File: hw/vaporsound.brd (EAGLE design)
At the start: 100 x 80 mm, 76 parts, among them Q1 BSS138, Q2 BSS138

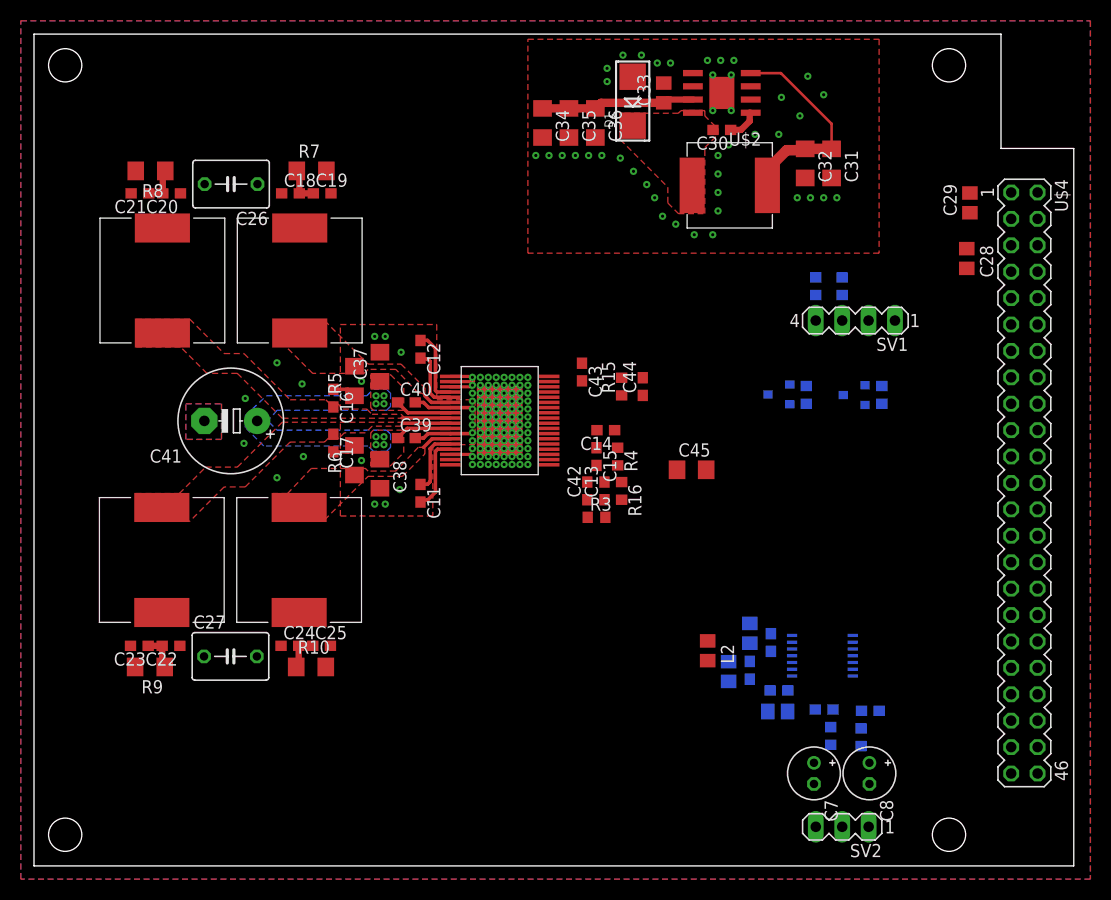
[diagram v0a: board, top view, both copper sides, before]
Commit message: output stage fully routed, adc routed
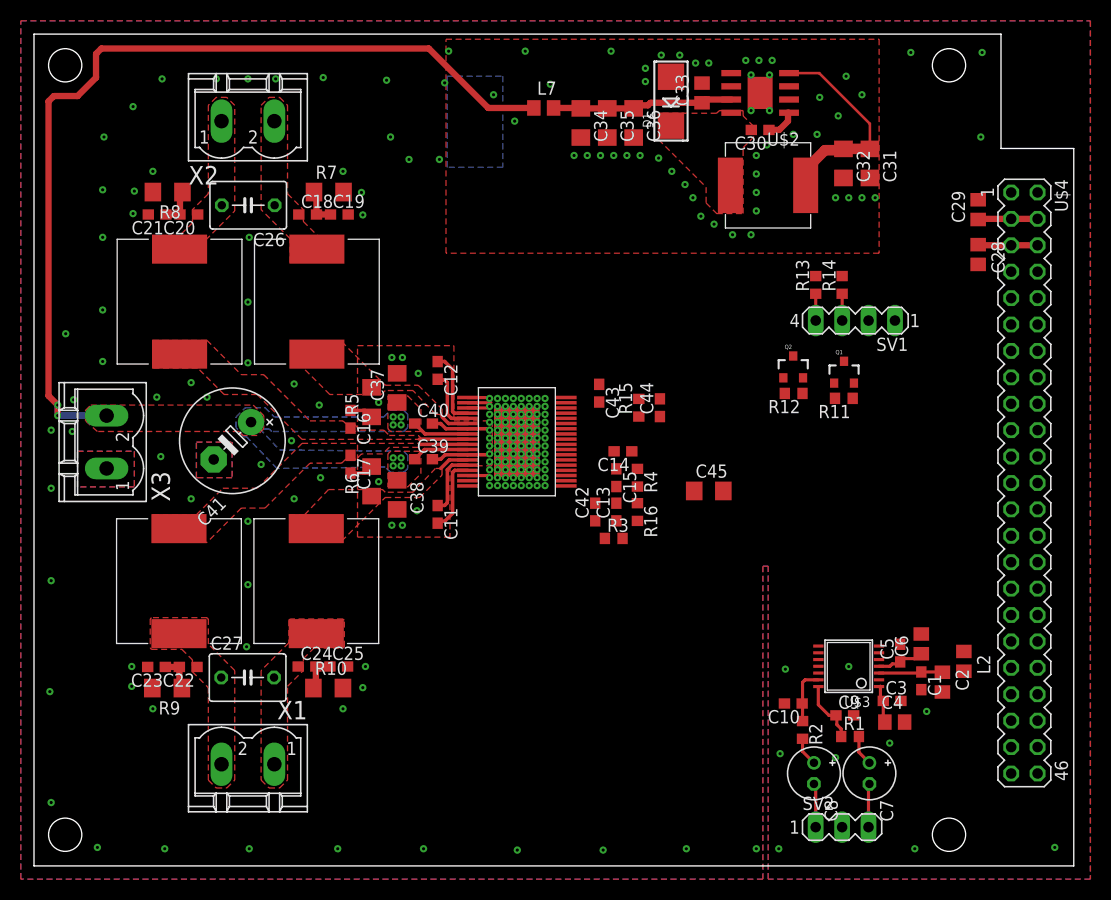
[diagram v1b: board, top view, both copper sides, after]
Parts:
- added L7: (no value), rcl:R0805
- added X1, X2, X3: MSTBV2, con-phoenix-508:MSTBV2
- moved L2 24.7 mm to (89.4, 19.7)
- moved C2 20.6 mm to (87.4, 17.7), flipped to the top
- moved C1 16.5 mm to (85.3, 17.8), flipped to the top
- moved C6 16.5 mm to (85.3, 21.4), flipped to the top
- moved C5 12.5 mm to (83.3, 20.5), flipped to the top
- moved C4 11.3 mm to (82.8, 13.8), flipped to the top
- moved C3 10.9 mm to (82.5, 15.9), flipped to the top
- moved C10 7.44 mm to (73.0, 15.6), flipped to the top
- moved R2 5.68 mm to (73.9, 13.1), flipped to the top
- moved C7 5.33 mm to (80.3, 8.90)
- moved C8 5.33 mm to (75.0, 8.90)
- moved C31 3.68 mm to (80.4, 67.6)
- moved C34 3.68 mm to (52.6, 71.5)
- moved C33 3.68 mm to (64.2, 74.3)
- moved C35 3.68 mm to (55.1, 71.5)
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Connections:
- new net 24V_DIGITAL: C33.1, C34.1, C35.1, C36.1, L7.2, U$2.7
- net +24V: now also L7.1, X3.2; no longer C33.1, C34.1, C35.1, C36.1, U$2.7
- net GND: now also X3.1
- net SPKR1A: now also X1.1
- net SPKR1B: now also X1.2
- net SPKR2A: now also X2.1
- net SPKR2B: now also X2.2
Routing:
- net +24V: track 25.8 -> 99.7 mm, vias 8 -> 10
- net 24V_DIGITAL: track 0.00 -> 17.5 mm
- net +3V3: track 0.00 -> 10.3 mm
- net V+: track 0.00 -> 6.15 mm
- net VIN_R: track 0.00 -> 6.11 mm
- net +5V: track 20.7 -> 26.5 mm
- net VIN_L: track 0.00 -> 5.38 mm
- net LEFT_INPUT: track 0.00 -> 4.22 mm
- net RIGHT_INPUT: track 0.00 -> 4.19 mm
- net ADC_VREF: track 0.00 -> 3.76 mm
- net C_RIGHT: track 0.00 -> 2.95 mm
- net C_LEFT: track 0.00 -> 2.77 mm
- net SDA5V: track 0.00 -> 2.58 mm
- net SCL5V: track 0.00 -> 2.58 mm
- net GND: vias 152 -> 226
- added copper zone on layer 1, net SPKR1A
- added copper zone on layer 1, net SPKR1B
- added copper zone on layer 1, net SPKR2A
- added copper zone on layer 1, net SPKR2B

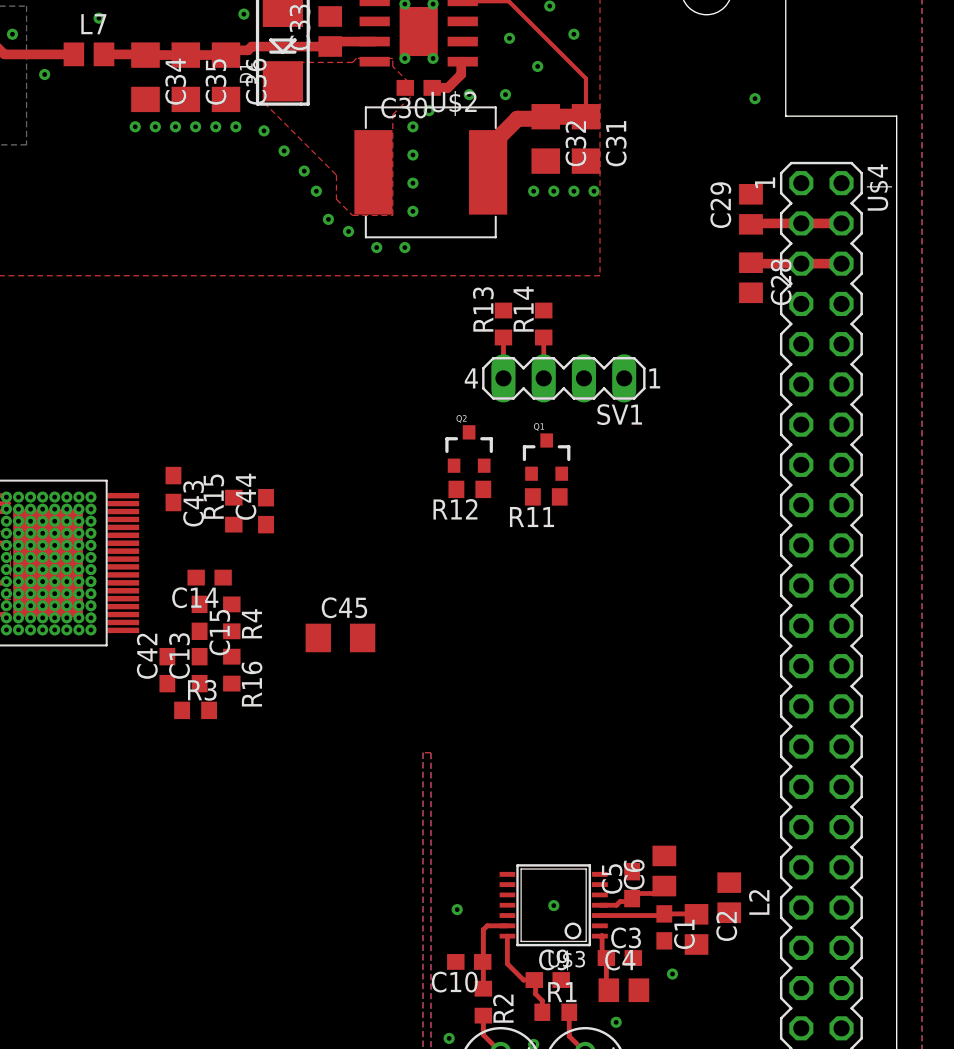
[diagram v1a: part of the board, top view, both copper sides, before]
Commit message: board fully routed
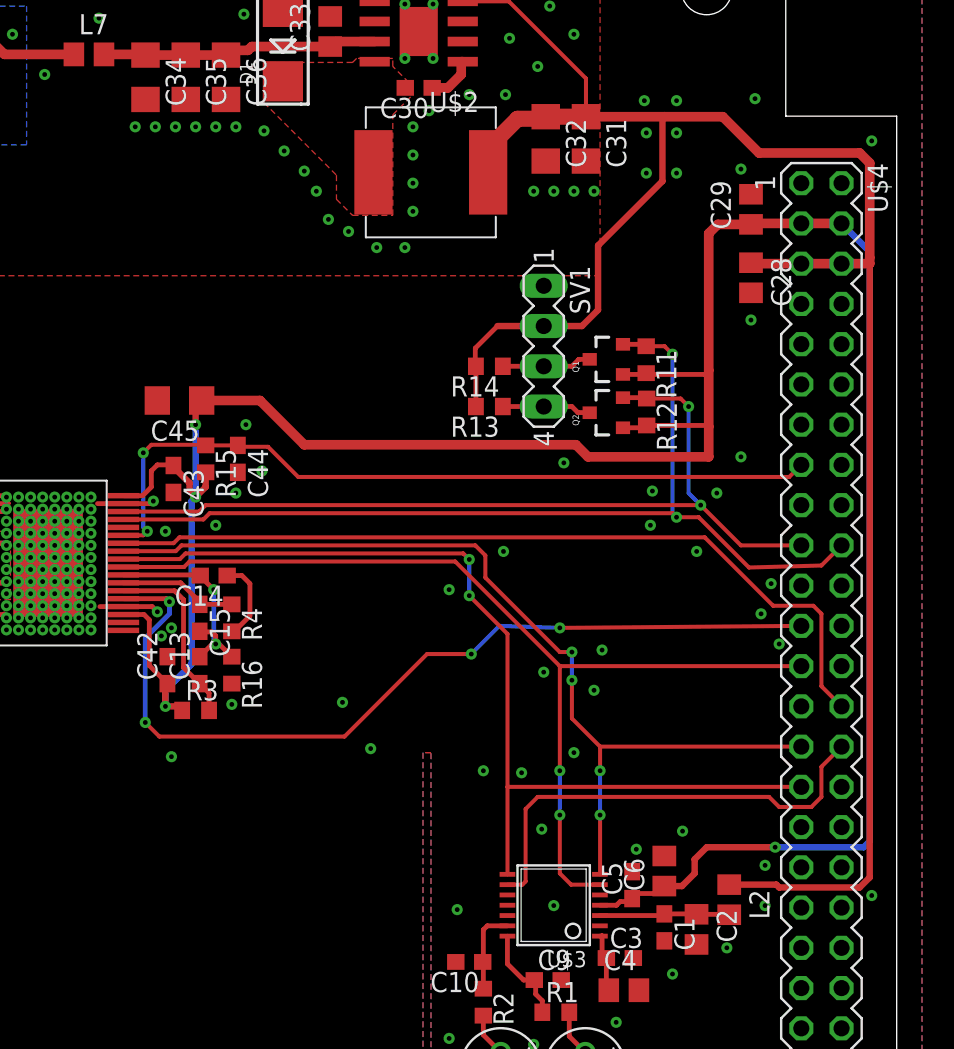
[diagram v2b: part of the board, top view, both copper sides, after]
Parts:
- moved C45 18.1 mm to (54.7, 51.1), turned to 180 degrees
- moved R12 12.2 mm to (84.2, 50.3), turned to 270 degrees
- moved R11 10.7 mm to (84.2, 53.6), turned to 270 degrees
- moved Q2 9.02 mm to (81.7, 50.3), turned to 90 degrees
- moved Q1 7.30 mm to (81.7, 53.6), turned to 90 degrees
- moved R13 5.28 mm to (74.3, 50.7), turned to 180 degrees
- moved R14 4.34 mm to (74.3, 53.2), turned to 180 degrees
- moved C44 3.75 mm to (58.4, 47.4), turned to 270 degrees
- moved R15 3.75 mm to (56.4, 47.4), turned to 270 degrees
- moved SV1 2.40 mm to (77.7, 54.5), turned to 270 degrees
- moved C43 0.63 mm to (54.4, 46.1)
- moved C14 0.28 mm to (56.9, 40.0)
- moved L2 0.13 mm to (89.4, 19.6)
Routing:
- net +3V3: track 10.3 -> 164.7 mm, vias 0 -> 4
- net +5V: track 26.5 -> 128.4 mm
- net MCK: track 0.00 -> 61.6 mm, vias 0 -> 2
- net BCK: track 0.00 -> 61.6 mm, vias 0 -> 2
- net SDA: track 0.00 -> 61.2 mm, vias 0 -> 2
- net LRCK: track 0.00 -> 59.5 mm, vias 0 -> 4
- net POWERDOWN: track 0.00 -> 55.9 mm, vias 0 -> 4
- net SCL: track 0.00 -> 54.9 mm, vias 0 -> 2
- net D_AMP: track 0.00 -> 52.6 mm
- net RESET: track 0.00 -> 49.6 mm, vias 0 -> 2
- net D_ADC: track 0.00 -> 29.0 mm
- net AGND: track 0.00 -> 13.9 mm, vias 0 -> 2
- net VDD_PLL: track 0.00 -> 11.7 mm
- net FILTER_PLL: track 0.00 -> 7.51 mm
- net GND: track 19.8 -> 27.2 mm, vias 226 -> 272
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
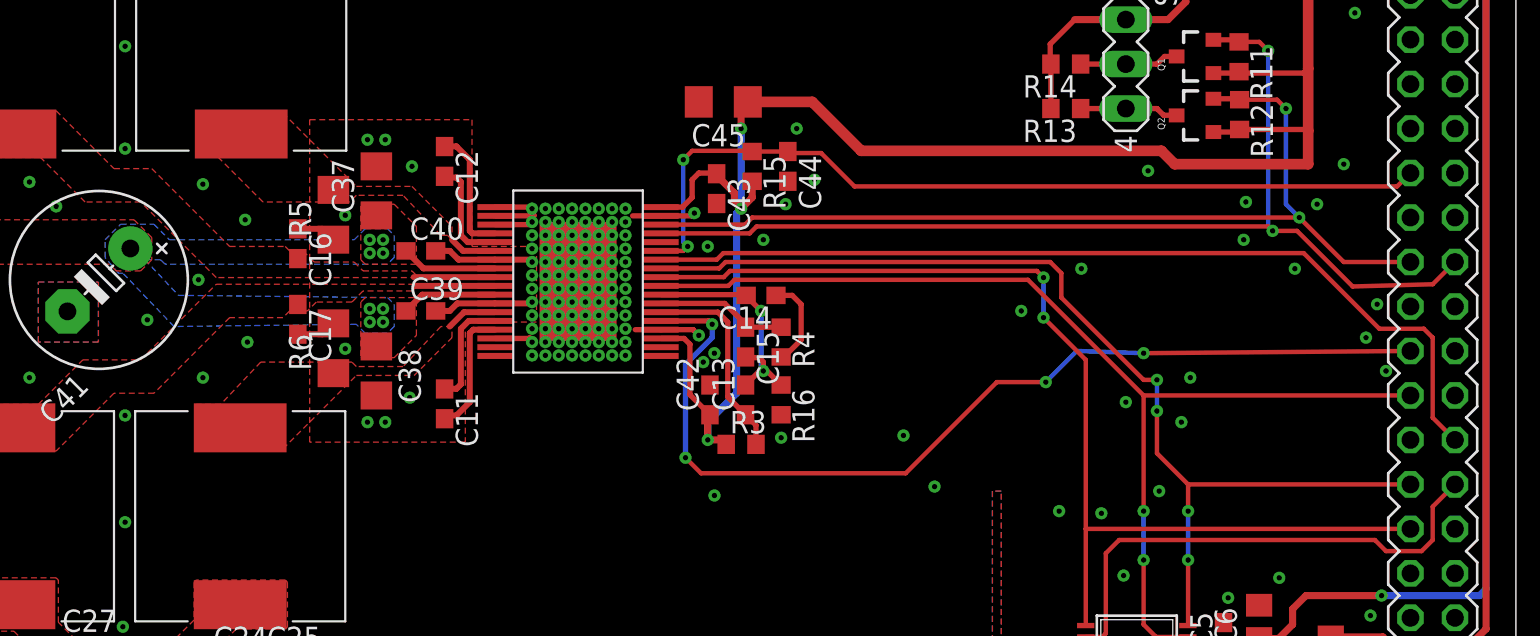
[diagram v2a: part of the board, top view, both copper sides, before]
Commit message: fix wrong angles
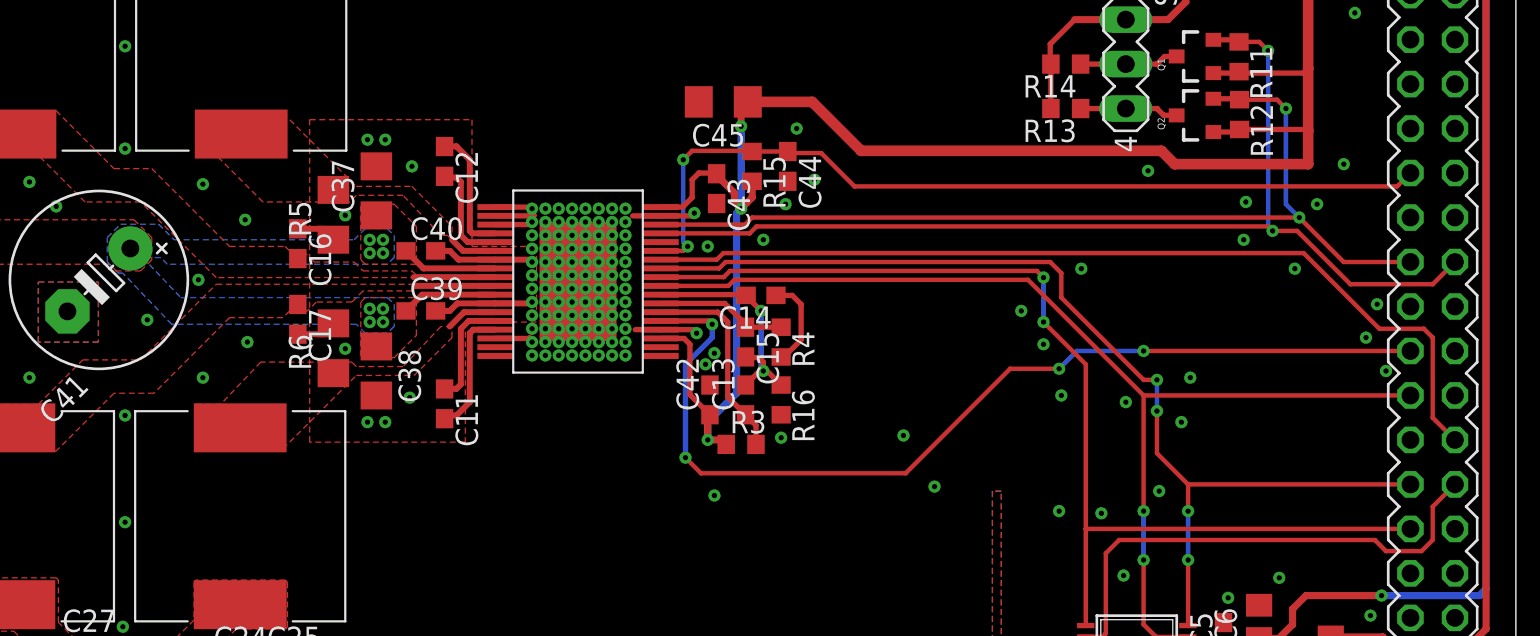
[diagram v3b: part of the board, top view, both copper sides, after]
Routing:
- net GND: track 27.2 -> 27.0 mm, vias 272 -> 274
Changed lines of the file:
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@@
 <via x="78.359" y="19.177" extent="1-16" drill="0.3"/>
 <via x="85.852" y="14.859" extent="1-16" drill="0.3"/>
-<via x="53.594" y="36.195" extent="1-16" drill="0.3"/>
-<via x="53.34" y="37.719" extent="1-16" drill="0.3"/>
+<via x="53.721" y="36.068" extent="1-16" drill="0.3"/>
+<via x="53.213" y="37.846" extent="1-16" drill="0.3"/>
 <via x="54.229" y="36.703" extent="1-16" drill="0.3"/>
 <wire x1="51.191" y1="38.046" x2="53.013" y2="38.046" width="0.3048" layer="1"/>
-<wire x1="53.013" y1="38.046" x2="53.34" y2="37.719" width="0.3048" layer="1"/>
+<wire x1="53.013" y1="38.046" x2="53.213" y2="37.846" width="0.3048" layer="1"/>
 <wire x1="49.711" y1="38.046" x2="51.191" y2="38.046" width="0.3048" layer="1"/>
 <via x="53.086" y="44.704" extent="1-16" drill="0.3"/>
@@
 <via x="66.802" y="29.083" extent="1-16" drill="0.3"/>
 <via x="65.024" y="32.004" extent="1-16" drill="0.3"/>
+<via x="74.041" y="34.29" extent="1-16" drill="0.3"/>
+<via x="73.025" y="37.211" extent="1-16" drill="0.3"/>
 </signal>
 <signal name="EPAD">
@@
 <wire x1="55.499" y1="34.417" x2="55.499" y2="44.704" width="0.4064" layer="16"/>
 <wire x1="55.499" y1="44.704" x2="55.753" y2="44.958" width="0.4064" layer="16"/>
-<wire x1="55.753" y1="44.958" x2="55.753" y2="49.53" width="0.4064" layer="16"/>
+<wire x1="55.753" y1="44.958" x2="55.753" y2="49.657" width="0.4064" layer="16"/>
 <via x="55.753" y="44.958" extent="1-16" drill="0.3"/>
 <wire x1="56.388" y1="46.521" x2="56.388" y2="45.593" width="0.4064" layer="1"/>
@@
 <wire x1="82.726" y1="52.699" x2="84.108" y2="52.699" width="0.3048" layer="1"/>
 <wire x1="84.108" y1="52.699" x2="84.19" y2="52.781" width="0.3048" layer="1"/>
-<via x="55.753" y="49.53" extent="1-16" drill="0.3"/>
+<via x="55.753" y="49.657" extent="1-16" drill="0.3"/>
 <wire x1="55.753" y1="44.958" x2="55.753" y2="45.173" width="0.4064" layer="1"/>
-<wire x1="55.753" y1="49.53" x2="55.753" y2="50.67" width="0.4064" layer="1"/>
+<wire x1="55.753" y1="49.657" x2="55.753" y2="50.67" width="0.4064" layer="1"/>
 <wire x1="55.753" y1="50.67" x2="56.137" y2="51.054" width="0.4064" layer="1"/>
 <wire x1="56.137" y1="51.054" x2="59.817" y2="51.054" width="0.6096" layer="1"/>
@@
 <wire x1="85.852" y1="43.942" x2="86.106" y2="43.688" width="0.254" layer="1"/>
 <wire x1="86.106" y1="43.688" x2="87.503" y2="43.688" width="0.254" layer="1"/>
-<wire x1="87.503" y1="43.688" x2="90.678" y2="40.513" width="0.254" layer="1"/>
-<wire x1="90.678" y1="40.513" x2="95.25" y2="40.64" width="0.254" layer="1"/>
 <wire x1="95.25" y1="40.64" x2="96.52" y2="41.91" width="0.254" layer="1"/>
 <wire x1="84.19" y1="54.481" x2="85.346" y2="54.481" width="0.254" layer="1"/>
@@
 <wire x1="85.852" y1="43.942" x2="86.106" y2="43.688" width="0.254" layer="16"/>
 <via x="86.106" y="43.688" extent="1-16" drill="0.3"/>
+<wire x1="87.503" y1="43.688" x2="90.551" y2="40.64" width="0.254" layer="1"/>
+<wire x1="90.551" y1="40.64" x2="95.25" y2="40.64" width="0.254" layer="1"/>
 </signal>
 <signal name="RESET">
@@
 <wire x1="54.102" y1="37.592" x2="52.578" y2="36.068" width="0.3048" layer="16"/>
 <wire x1="52.578" y1="36.068" x2="52.578" y2="30.734" width="0.3048" layer="16"/>
-<wire x1="93.98" y1="36.83" x2="78.74" y2="36.703" width="0.254" layer="1"/>
+<wire x1="93.98" y1="36.83" x2="78.74" y2="36.83" width="0.254" layer="1"/>
 <via x="52.578" y="30.734" extent="1-16" drill="0.3"/>
 <wire x1="52.578" y1="30.734" x2="53.467" y2="29.845" width="0.254" layer="1"/>
 <wire x1="53.467" y1="29.845" x2="65.151" y2="29.845" width="0.254" layer="1"/>
-<via x="78.74" y="36.703" extent="1-16" drill="0.3"/>
-<wire x1="78.74" y1="36.703" x2="74.93" y2="36.83" width="0.254" layer="16"/>
-<wire x1="74.93" y1="36.83" x2="73.152" y2="35.052" width="0.254" layer="16"/>
-<via x="73.152" y="35.052" extent="1-16" drill="0.3"/>
-<wire x1="73.152" y1="35.052" x2="70.358" y2="35.052" width="0.254" layer="1"/>
-<wire x1="70.358" y1="35.052" x2="65.151" y2="29.845" width="0.254" layer="1"/>
+<via x="78.74" y="36.83" extent="1-16" drill="0.3"/>
+<wire x1="78.74" y1="36.83" x2="74.93" y2="36.83" width="0.254" layer="16"/>
+<wire x1="74.93" y1="36.83" x2="73.914" y2="35.814" width="0.254" layer="16"/>
+<via x="73.914" y="35.814" extent="1-16" drill="0.3"/>
+<wire x1="73.914" y1="35.814" x2="71.12" y2="35.814" width="0.254" layer="1"/>
+<wire x1="71.12" y1="35.814" x2="65.151" y2="29.845" width="0.254" layer="1"/>
 </signal>
 <signal name="D_AMP">
@@
 <wire x1="72.644" y1="41.402" x2="73.025" y2="41.021" width="0.254" layer="1"/>
 <via x="73.025" y="41.021" extent="1-16" drill="0.3"/>
-<wire x1="73.025" y1="41.021" x2="73.025" y2="38.735" width="0.254" layer="16"/>
-<via x="73.025" y="38.735" extent="1-16" drill="0.3"/>
-<wire x1="73.025" y1="38.735" x2="75.438" y2="36.322" width="0.254" layer="1"/>
-<wire x1="75.438" y1="36.322" x2="75.438" y2="26.67" width="0.254" layer="1"/>
+<wire x1="73.025" y1="41.021" x2="73.025" y2="38.481" width="0.254" layer="16"/>
+<via x="73.025" y="38.481" extent="1-16" drill="0.3"/>
+<wire x1="73.025" y1="38.481" x2="75.438" y2="36.068" width="0.254" layer="1"/>
+<wire x1="75.438" y1="36.068" x2="75.438" y2="26.67" width="0.254" layer="1"/>
 <wire x1="75.438" y1="26.67" x2="75.438" y2="21.1538" width="0.254" layer="1"/>
 <wire x1="75.438" y1="21.1538" x2="75.4332" y2="21.149" width="0.254" layer="1"/>
@@
 <vertex x="35.941" y="42.164"/>
 <vertex x="35.56" y="41.783"/>
-<vertex x="22.86" y="41.783"/>
-<vertex x="22.606" y="42.037"/>
-<vertex x="21.717" y="42.037"/>
-<vertex x="23.622" y="40.005"/>
+<vertex x="22.987" y="41.783"/>
+<vertex x="22.606" y="42.164"/>
+<vertex x="21.59" y="42.164"/>
+<vertex x="23.749" y="39.878"/>
 <vertex x="35.56" y="39.878"/>
 <vertex x="35.941" y="39.497"/>
@@
 <vertex x="34.29" y="37.846"/>
 <vertex x="33.782" y="38.354"/>
-<vertex x="23.368" y="38.227"/>
+<vertex x="23.241" y="38.354"/>
 <vertex x="20.447" y="41.275"/>
 <vertex x="20.193" y="41.275"/>
-<vertex x="19.431" y="42.164"/>
-<vertex x="19.431" y="43.18"/>
+<vertex x="19.558" y="41.91"/>
+<vertex x="19.558" y="43.307"/>
 <vertex x="20.32" y="44.069"/>
-<vertex x="22.225" y="44.069"/>
-<vertex x="23.114" y="43.18"/>
+<vertex x="22.479" y="44.069"/>
+<vertex x="23.368" y="43.18"/>
 <vertex x="33.655" y="43.18"/>
 </polygon>
